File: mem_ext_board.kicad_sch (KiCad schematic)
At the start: 13 parts, among them J1 Conn_02x05_Odd_Even, J2 Conn_02x02_Odd_Even, J3 Conn_02x16_Row_Letter_First, U1 74LS30, U2 AS6C1008-xxT, U4 74LS86

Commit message: Updated board to hopefully final shape
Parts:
- added J4: Conn_02x05_Odd_Even, Connector_PinSocket_2.54mm:PinSocket_2x05_P2.54mm_Vertical, symbol Connector_Generic:Conn_02x05_Odd_Even
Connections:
- net +5V: now also J4.2 (Pin_2)
- net A16: now also J4.10 (Pin_10)
- net A17: now also J4.9 (Pin_9)
- net A18: now also J4.8 (Pin_8)
- net A19: now also J4.7 (Pin_7)
- net A20: now also J4.6 (Pin_6)
- net A21: now also J4.5 (Pin_5)
- net GND: now also J4.1 (Pin_1), J4.3 (Pin_3), J4.4 (Pin_4)
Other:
- moved on the sheet: J1

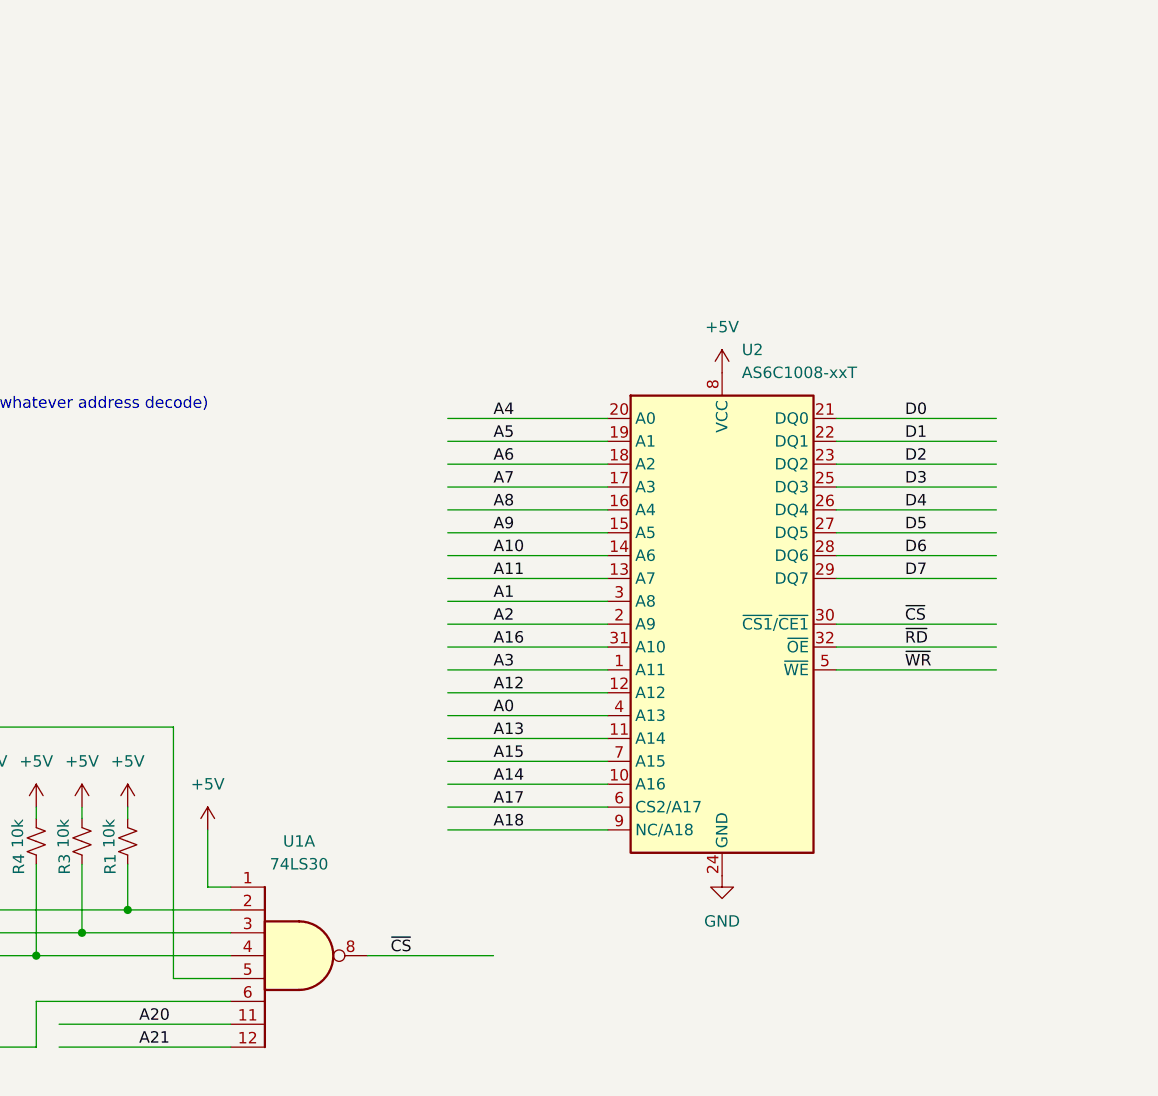
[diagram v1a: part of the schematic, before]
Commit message: Added support for 1Mbit part, release package added.
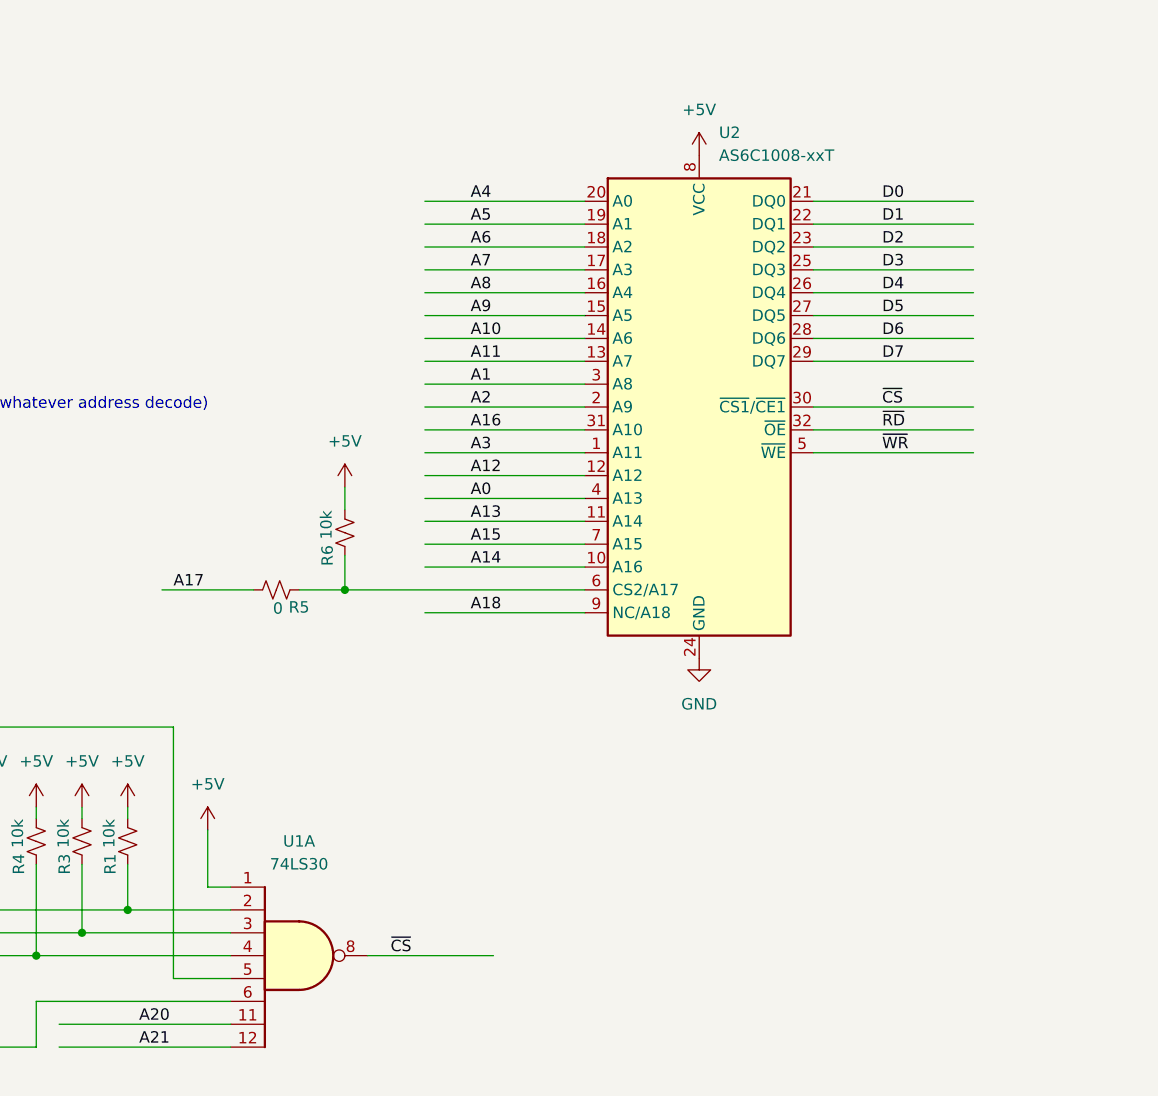
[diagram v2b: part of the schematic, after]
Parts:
- added R5: 0, Resistor_SMD:R_0603_1608Metric_Pad0.98x0.95mm_HandSolder, symbol Device:R_Small_US
- added R6: 10k, Resistor_SMD:R_0603_1608Metric_Pad0.98x0.95mm_HandSolder, symbol Device:R_Small_US
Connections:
- net +5V: now also R6.1
- net A17: now also R5.1; no longer U2.6 (CS2/A17)
- new net: R5.2, R6.2, U2.6 (CS2/A17)
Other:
- moved on the sheet: U2

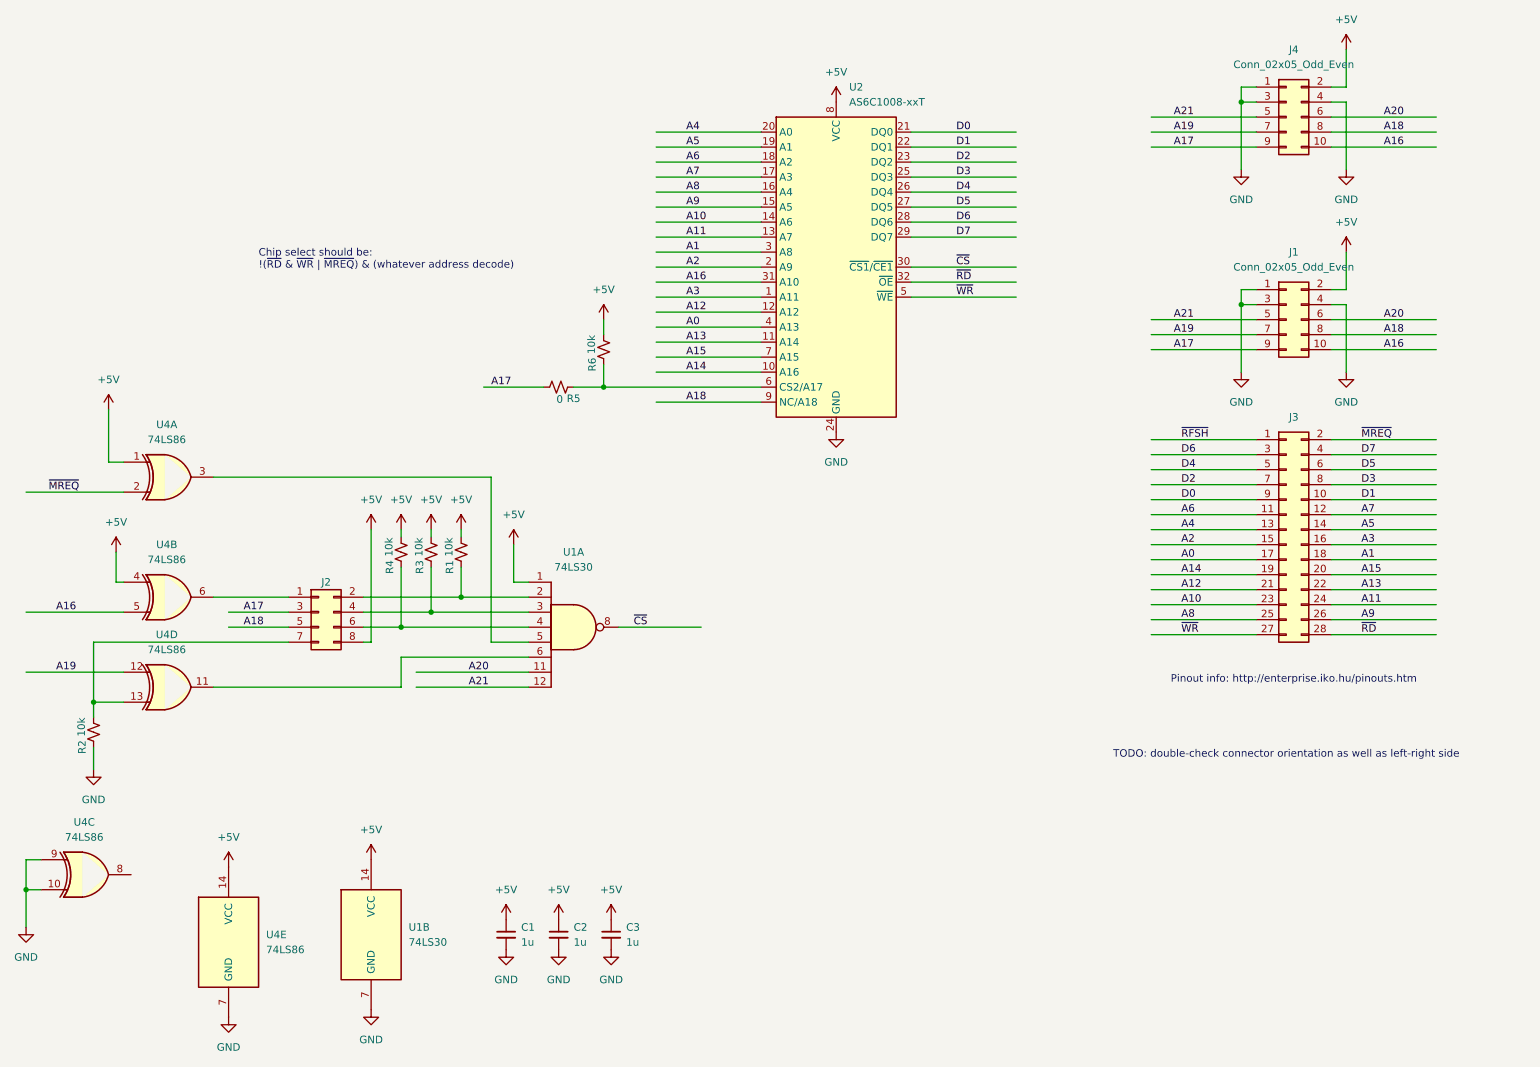
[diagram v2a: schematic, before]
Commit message: Universal memory footprint added: multiple package sizes are supported.
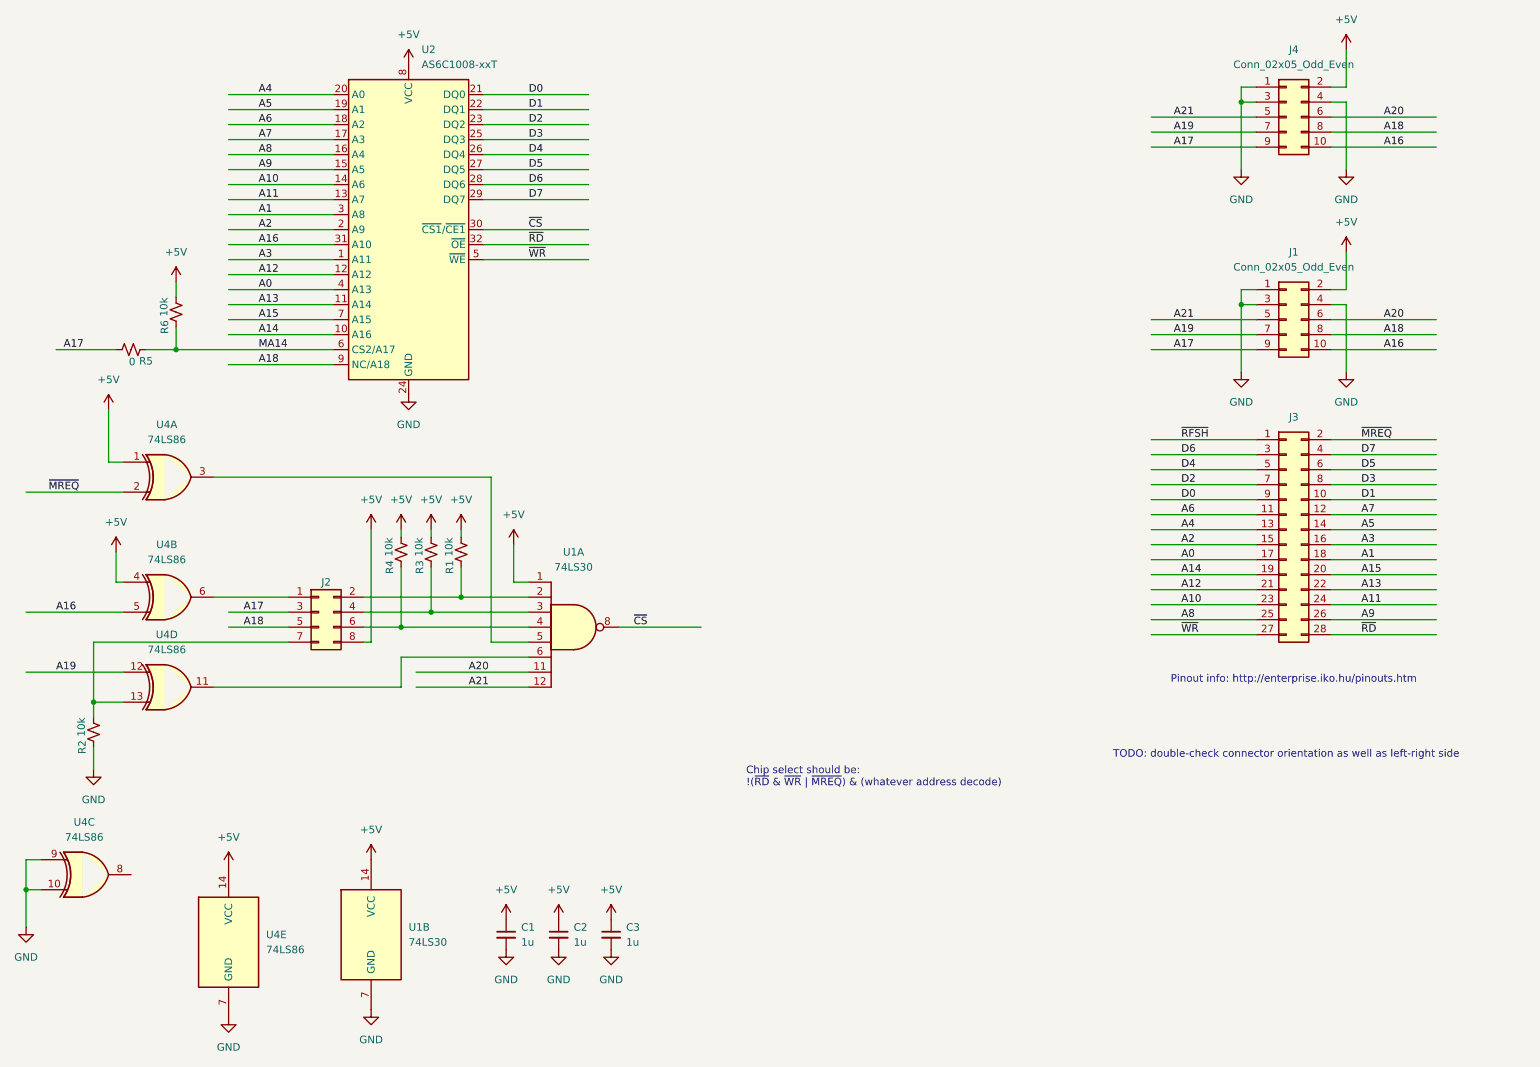
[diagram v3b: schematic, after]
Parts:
- U2: footprint Package_SO:TSOP-I-32_18.4x8mm_P0.5mm -> mem_ext_board:TSOP-I-32_11-18.4x8mm_P0.5mm
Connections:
- net MA14: now reaches R5.2, R6.2, U2.6 (CS2/A17)
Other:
- moved on the sheet: R5, R6, U2

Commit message: Flipped jumper setting so that operation matches silk-screen.
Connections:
- net +5V: now also R2.1; no longer J2.8 (Pin_8)
- net GND: now also J2.8 (Pin_8); no longer R2.2
- net at J2.7 (Pin_7), U4.13: now also R2.2; no longer R2.1
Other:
- moved on the sheet: R2
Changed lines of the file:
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@@
 	)
 	(junction
-		(at 53.34 71.12)
+		(at 39.37 120.65)
 		(diameter 0)
 		(color 0 0 0 0)
 	)
 	(junction
-		(at 233.68 29.21)
+		(at 53.34 71.12)
 		(diameter 0)
 		(color 0 0 0 0)
 	)
 	(junction
-		(at 39.37 130.81)
+		(at 233.68 29.21)
 		(diameter 0)
 		(color 0 0 0 0)
@@
 	(wire
 		(pts
-			(xy 86.36 101.6) (xy 86.36 120.65)
+			(xy 218.44 31.75) (xy 236.22 31.75)
 		)
 		(stroke
@@
 	(wire
 		(pts
-			(xy 218.44 31.75) (xy 236.22 31.75)
+			(xy 251.46 63.5) (xy 251.46 74.93)
 		)
 		(stroke
@@
 	(wire
 		(pts
-			(xy 251.46 63.5) (xy 251.46 74.93)
+			(xy 233.68 63.5) (xy 236.22 63.5)
 		)
 		(stroke
@@
 	(wire
 		(pts
-			(xy 233.68 63.5) (xy 236.22 63.5)
+			(xy 27.94 125.73) (xy 44.45 125.73)
 		)
 		(stroke
@@
 	(wire
 		(pts
-			(xy 27.94 125.73) (xy 44.45 125.73)
+			(xy 39.37 111.76) (xy 39.37 120.65)
 		)
 		(stroke
@@
 	(wire
 		(pts
-			(xy 39.37 138.43) (xy 39.37 142.24)
-		)
-		(stroke
-			(width 0)
-			(type default)
-		)
-	)
-	(wire
-		(pts
 			(xy 105.41 38.1) (xy 123.19 38.1)
 		)
@@
 	(wire
 		(pts
+			(xy 39.37 105.41) (xy 39.37 106.68)
+		)
+		(stroke
+			(width 0)
+			(type default)
+		)
+	)
+	(wire
+		(pts
 			(xy 91.44 101.6) (xy 91.44 102.87)
 		)
@@
 	(wire
 		(pts
-			(xy 39.37 130.81) (xy 39.37 133.35)
-		)
-		(stroke
-			(width 0)
-			(type default)
-		)
-	)
-	(wire
-		(pts
 			(xy 62.23 118.11) (xy 72.39 118.11)
 		)
@@
 	(wire
 		(pts
+			(xy 86.36 120.65) (xy 86.36 138.43)
+		)
+		(stroke
+			(width 0)
+			(type default)
+		)
+	)
+	(wire
+		(pts
 			(xy 248.92 101.6) (xy 266.7 101.6)
 		)
@@
 	(symbol
 		(lib_id "power:GND")
-		(at 39.37 142.24 0)
+		(at 86.36 138.43 0)
 		(unit 1)
 		(exclude_from_sim no)
@@
 		(fields_autoplaced yes)
 		(property "Reference" "#PWR012"
-			(at 39.37 148.59 0)
+			(at 86.36 144.78 0)
 			(effects
 				(font
@@
 		)
 		(property "Value" "GND"
-			(at 39.37 147.32 0)
+			(at 86.36 143.51 0)
 			(effects
 				(font
@@
 		)
 		(property "Footprint" ""
-			(at 39.37 142.24 0)
+			(at 86.36 138.43 0)
 			(effects
 				(font
@@
 		)
 		(property "Datasheet" ""
-			(at 39.37 142.24 0)
+			(at 86.36 138.43 0)
 			(effects
 				(font
@@
 		)
 		(property "Description" "Power symbol creates a global label with name \"GND\" , ground"
-			(at 39.37 142.24 0)
+			(at 86.36 138.43 0)
 			(effects
 				(font
@@
 	(symbol
 		(lib_id "Device:R_Small_US")
-		(at 39.37 135.89 0)
+		(at 39.37 109.22 0)
 		(unit 1)
 		(exclude_from_sim no)
@@
 		(dnp no)
 		(property "Reference" "R2"
-			(at 37.4369 139.578 90)
+			(at 37.4369 112.908 90)
 			(effects
 				(font
@@
 		)
 		(property "Value" "10k"
-			(at 37.3121 136.6258 90)
+			(at 37.3121 109.9558 90)
 			(effects
 				(font
@@
 		)
 		(property "Footprint" "Resistor_SMD:R_0603_1608Metric_Pad0.98x0.95mm_HandSolder"
-			(at 39.37 135.89 0)
+			(at 39.37 109.22 0)
 			(effects
 				(font
@@
 		)
 		(property "Datasheet" "~"
-			(at 39.37 135.89 0)
+			(at 39.37 109.22 0)
 			(effects
 				(font
@@
 		)
 		(property "Description" "Resistor, small US symbol"
-			(at 39.37 135.89 0)
+			(at 39.37 109.22 0)
 			(effects
 				(font
@@
 	(symbol
 		(lib_id "power:+5V")
-		(at 86.36 101.6 0)
+		(at 39.37 105.41 0)
 		(unit 1)
 		(exclude_from_sim no)
@@
 		(fields_autoplaced yes)
 		(property "Reference" "#PWR011"
-			(at 86.36 105.41 0)
+			(at 39.37 109.22 0)
 			(effects
 				(font
@@
 		)
 		(property "Value" "+5V"
-			(at 86.36 96.52 0)
+			(at 39.37 100.33 0)
 			(effects
 				(font
@@
 		)
 		(property "Footprint" ""
-			(at 86.36 101.6 0)
+			(at 39.37 105.41 0)
 			(effects
 				(font
@@
 		)
 		(property "Datasheet" ""
-			(at 86.36 101.6 0)
+			(at 39.37 105.41 0)
 			(effects
 				(font
@@
 		)
 		(property "Description" "Power symbol creates a global label with name \"+5V\""
-			(at 86.36 101.6 0)
+			(at 39.37 105.41 0)
 			(effects
 				(font
